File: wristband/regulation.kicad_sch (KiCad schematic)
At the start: 3 parts, among them U5 MCP1700T-3302E/TT

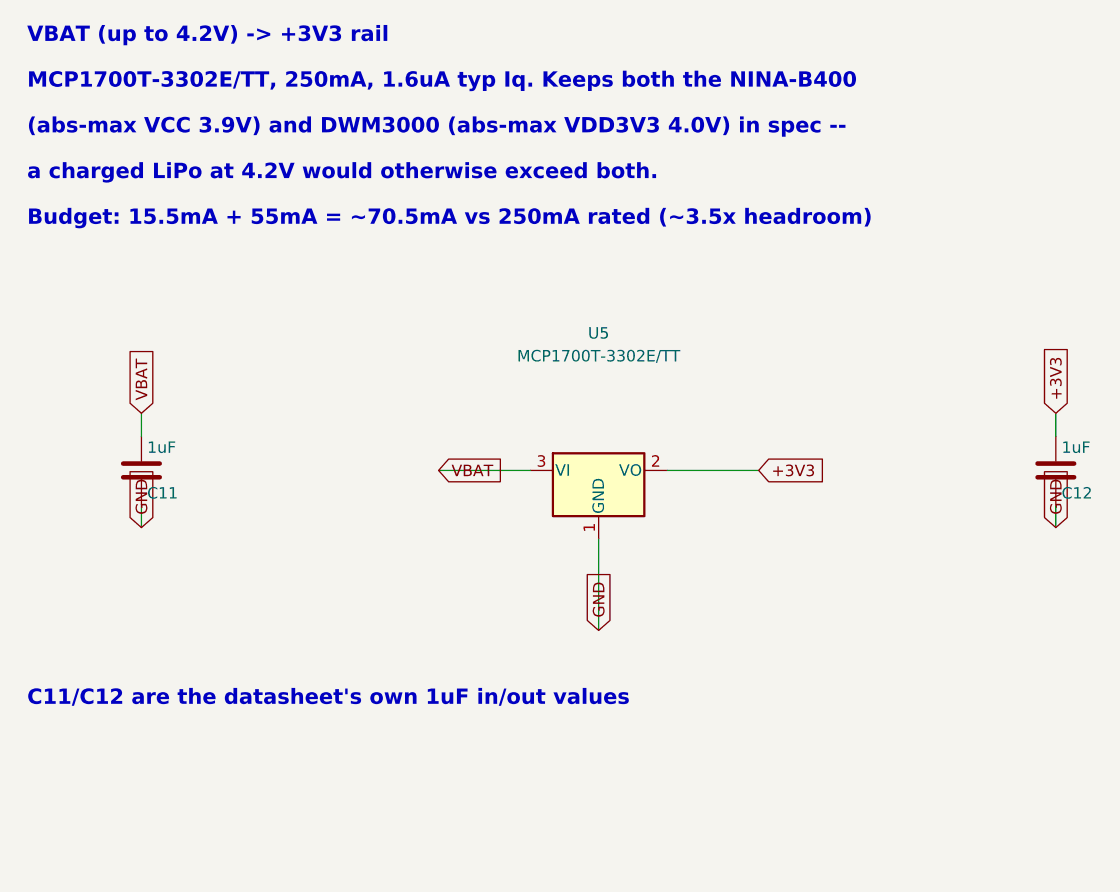
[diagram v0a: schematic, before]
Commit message: Convert global labels to power symbols; import footprints to PCB
Continues the ground cleanup from 0263e7f across the rest of the wristband
sheets: global labels replaced with explicit power symbols and wired
junctions, so connections are drawn rather than implied by name.

                     wires      labels      junctions   symbols
  power_bms          61 -> 83   61 -> 51    0 -> 3      25 -> 36
  programming_debug   7 ->  8    7 ->  4    0 -> 1       1 ->  3
  radio_mcu          71 -> 79   64 -> 42    7 -> 17     18 -> 32
  regulation          7 ->  7    7 ->  4    0 -> 0       3 ->  6

The added symbols are all power ports, so the BOM is untouched: still 47
components, 76 nets, 42 no-connects, 35 analyzer findings with 1 error --
identical before and after. The one error is the known DW01A false
positive (U1.6 GND sits on CELL_N by design, per the reference circuit).

Also ran Update PCB from Schematic on the wristband: 0 -> 46 footprints.
Nothing routed yet, no zones, board outline unchanged.

Co-Authored-By: Claude Opus 5 (1M context) <noreply@anthropic.com>
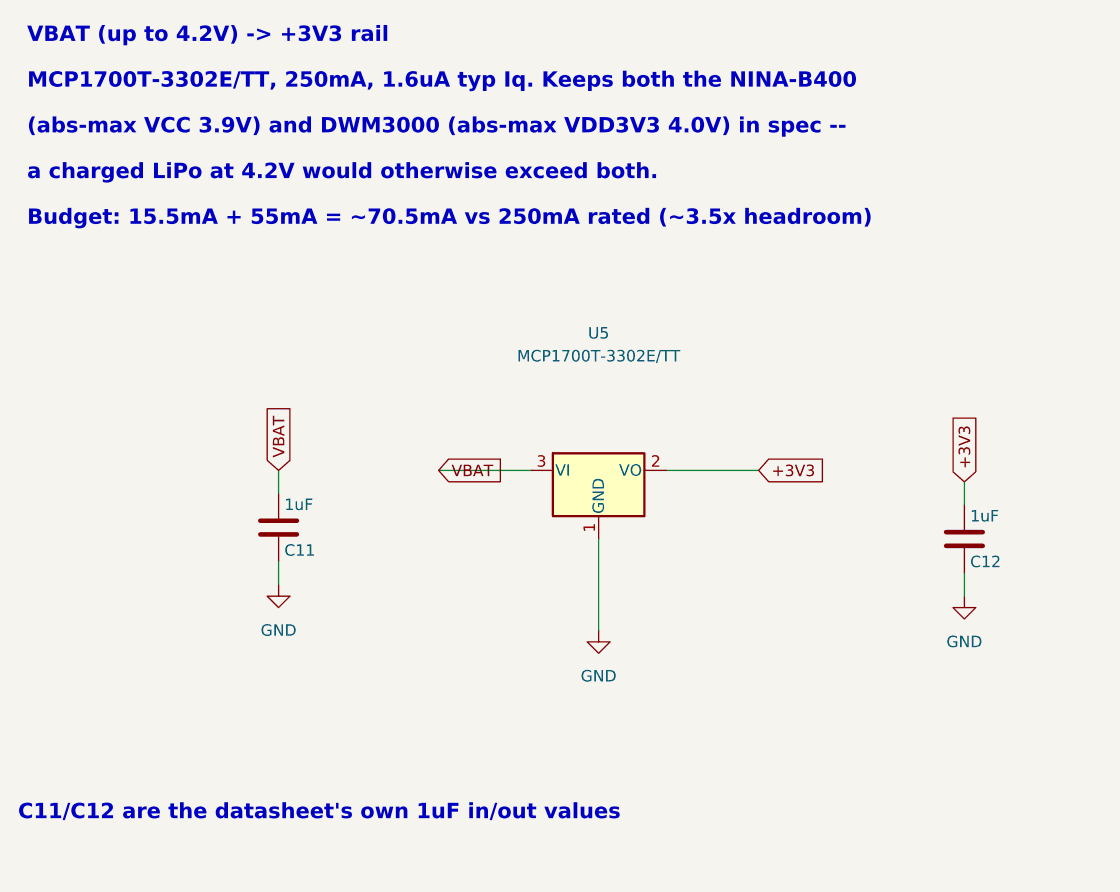
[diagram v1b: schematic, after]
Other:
- moved on the sheet: C11, C12

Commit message: Migrate wristband to DWM3001C; swap LDO to TPS7A02; fix ERC
Replace the NINA-B400 + DWM3000 pair with a single Qorvo DWM3001C, then
replace the MCP1700 LDO with a nanopower TI TPS7A0233. Wristband ERC goes
from 1 error / 13 warnings to 0 errors / 1 warning.

DWM3001C (U4), verified against Qorvo DS Rev B May 2022:
- Integrates DW3110 UWB + nRF52833 BLE MCU + LIS2DH12 + UWB antenna +
  Bluetooth chip antenna + 38.4MHz crystal. Its nRF52833 is now the host,
  so U3 (NINA-B400) is deleted.
- The DW3110<->nRF52833 SPI is internal, so the board-level UWB SPI bus,
  IRQ/RSTn/WAKEUP, the GPIO5/6 SPI-mode straps (R7/R8), the IRQ pulldown
  (R9) and the external LFXO (Y1/C14/C15) are all gone. C8-C10 too.
- AE1 (PRO-IS-237) removed: the module carries both antennas, so
  antenna.kicad_sch is documentation-only and places nothing.
- SWD moved for the first time: SWD_CLK=2, SWD_DIO=3, RESET=47 (P0.18),
  SWO=28 (P1.00). Battery sense moved to P0.02 = AIN0. Both P1.00=SWO and
  P0.02=AIN0 confirmed in nRF52833 PS v1.7 p825-826.
- Symbol + DWM3001C_PLACEHOLDER footprint are wristband-only, in libs/.
  The footprint has TWO unresolved dimensions (side pitch back-derives to
  1.06375mm; bottom pad row width undimensioned and apparently off-centre).
  VERIFY BEFORE FAB.

TPS7A0233PDBVR (U5), verified against TI SBVS277C:
- Iq 1.6uA typ / 4uA max -> 25nA typ / 46nA max; it was the largest single
  standby draw, bigger than the DWM3001C's own 850nA sleep. Board standby
  ~4.3uA -> ~2.7uA. Accuracy +/-1.5% vs +/-2.5%.
- Not a drop-in: SOT-23-5 1=IN 2=GND 3=EN 4=NC 5=OUT. EN ties to VBAT
  because TPS7A02 is disabled when EN floats and the MCU on this rail
  cannot enable its own supply.
- C12 1uF -> 2.2uF for the 0.5uF effective-capacitance stability floor.
- Symbol is self-contained: KiCad ships no TPS7A02, and every TPS7A05
  sibling is extends-based, which kicad-cli cannot load.

ERC fixes:
- Real bug: regulation.kicad_sch had no labels at all, so U5's input and
  C11 sat on an iso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
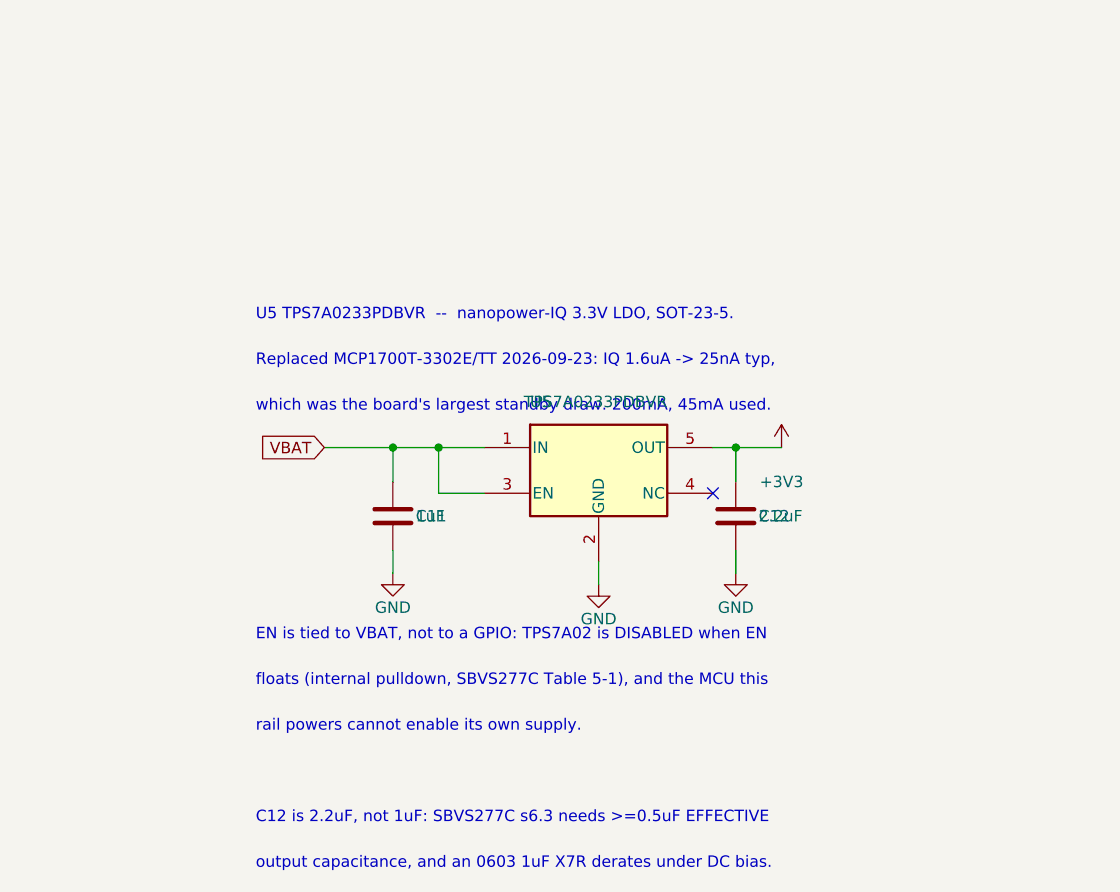
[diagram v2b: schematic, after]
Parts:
- removed U5: MCP1700T-3302E/TT, Package_TO_SOT_SMD:SOT-23, symbol Regulator_Linear:MCP1700x-330xxTT
- added U5: TPS7A0233PDBVR, Package_TO_SOT_SMD:SOT-23-5, symbol wristband:TPS7A0233PDBVR
- C12: value 1uF -> 2.2uF
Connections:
- net +3V3: now also U5.5 (OUT)
- net GND: now also U5.2 (GND)
- net VBAT: now also U5.1 (IN), U5.3 (EN)
- no-connect marks 0 -> 1
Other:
- note added: "C12 is 2.2uF, not 1uF: SBVS277C s6.3 needs >=0.5uF EFFECTIVE"
- note added: "EN is tied to VBAT, not to a GPIO: TPS7A02 is DISABLED when EN"
- note added: "Replaced MCP1700T-3302E/TT 2026-09-23: IQ 1.6uA -> 25nA typ,"
- note added: "U5 TPS7A0233PDBVR -- nanopower-IQ 3.3V LDO, SOT-23-5."
- note added: "floats (internal pulldown, SBVS277C Table 5-1), and the MCU this"
- note added: "output capacitance, and an 0603 1uF X7R derates under DC bias."
- note added: "rail powers cannot enable its own supply."
- note added: "which was the board's largest standby draw. 200mA, 45mA used."
- note removed: "(abs-max VCC 3.9V) and DWM3000 (abs-max VDD3V3 4.0V) in spec --"
- note removed: "Budget: 15.5mA + 55mA = ~70.5mA vs 250mA rated (~3.5x headroom)"
- note removed: "C11/C12 are the datasheet's own 1uF in/out values"
- note removed: "MCP1700T-3302E/TT, 250mA, 1.6uA typ Iq. Keeps both the NINA-B400"
- note removed: "VBAT (up to 4.2V) -> +3V3 rail"
- note removed: "a charged LiPo at 4.2V would otherwise exceed both."
- moved on the sheet: C11, C12
